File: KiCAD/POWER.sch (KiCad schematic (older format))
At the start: 9 parts, among them J35 Conn_01x02, J36 Conn_01x02, T1 da2303, U12 SN6505A

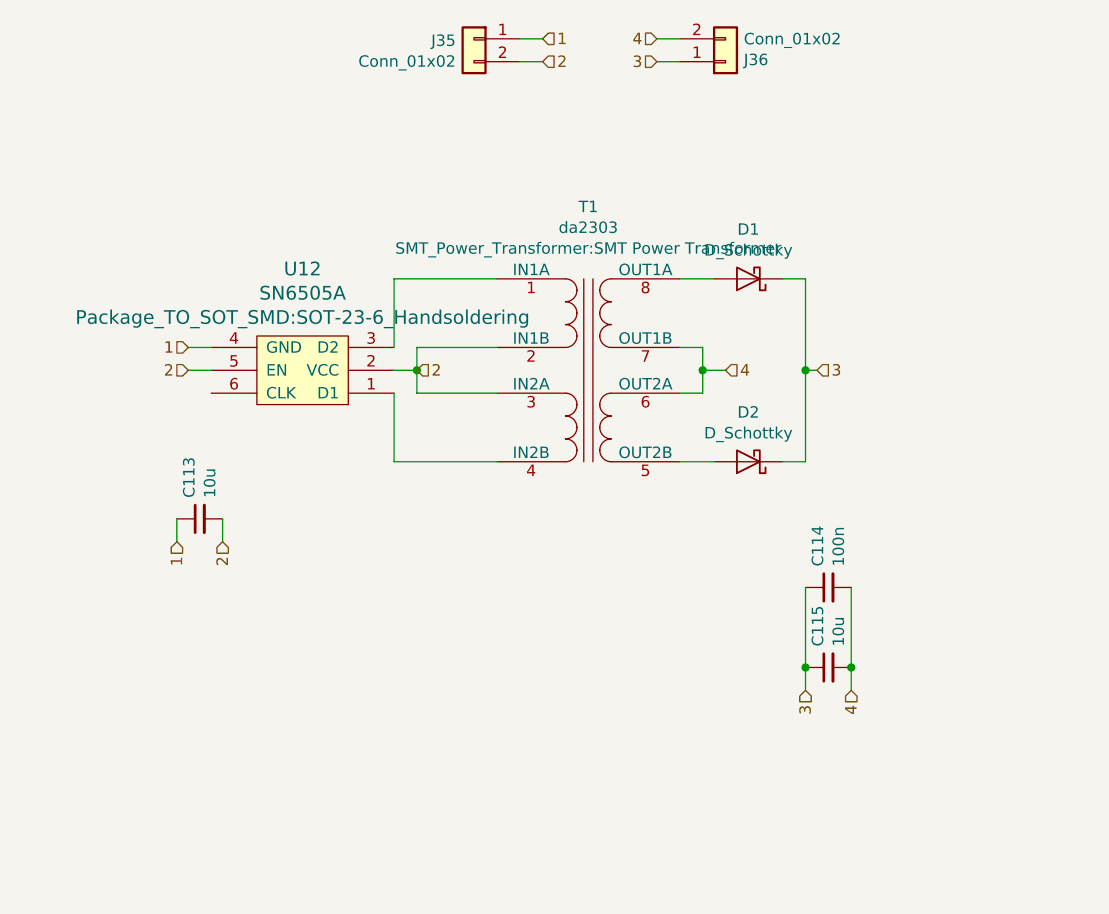
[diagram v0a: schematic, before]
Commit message: added usb, crystals
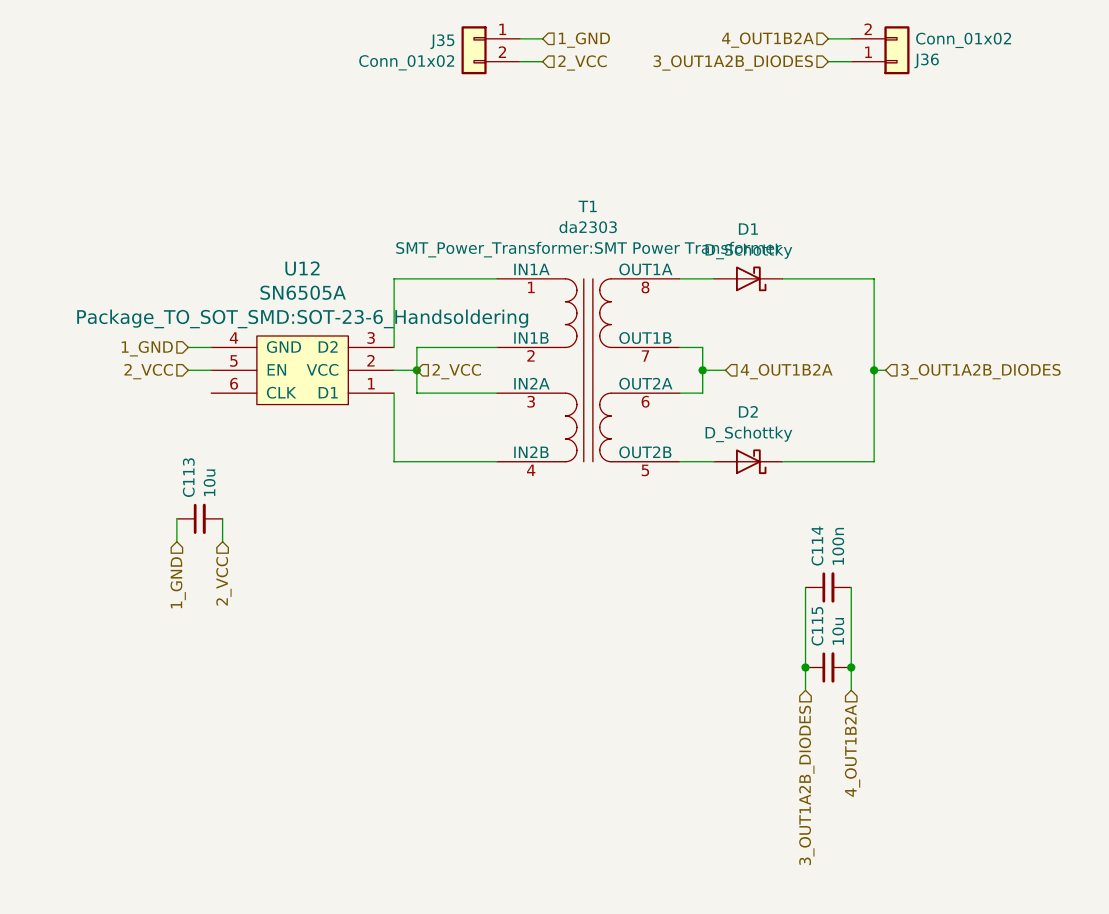
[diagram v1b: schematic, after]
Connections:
- net 1 renamed 1_GND
- net 2 renamed 2_VCC
- net 3 renamed 3_OUT1A2B_DIODES
- net 4 renamed 4_OUT1B2A
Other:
- moved on the sheet: J36
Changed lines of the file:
@@
 $Descr A4 11693 8268
 encoding utf-8
-Sheet 13 17
+Sheet 12 18
 Title ""
 Date ""
@@
 $EndComp
 Text HLabel 5350 4650 3    50   Input ~ 0
-3
+3_OUT1A2B_DIODES
 Text HLabel 5550 4650 3    50   Input ~ 0
-4
+4_OUT1B2A
 $Comp
 L Device:C_Small C?
@@
 Connection ~ 5550 4550
 Text HLabel 2600 4000 3    50   Input ~ 0
-1
+1_GND
 Text HLabel 2800 4000 3    50   Input ~ 0
-2
+2_VCC
 $Comp
 L Device:C_Small C?
@@
 L Connector_Generic:Conn_01x02 J?
 U 1 1 5CDCDD1E
-P 5000 1900
+P 5750 1900
 AR Path="/5CDAD75F/5CDCDD1E" Ref="J?"  Part="1"
 AR Path="/5CDCD748/5CDCDD1E" Ref="J36"  Part="1"
-F 0 "J36" H 5080 1892 50  0000 L CNN
-F 1 "Conn_01x02" H 5080 1801 50  0000 L CNN
-F 2 "Connector_PinHeader_2.54mm:PinHeader_1x02_P2.54mm_Vertical" H 5000 1900 50  0001 C CNN
-F 3 "~" H 5000 1900 50  0001 C CNN
-	1    5000 1900
+F 0 "J36" H 5830 1892 50  0000 L CNN
+F 1 "Conn_01x02" H 5830 1801 50  0000 L CNN
+F 2 "Connector_PinHeader_2.54mm:PinHeader_1x02_P2.54mm_Vertical" H 5750 1900 50  0001 C CNN
+F 3 "~" H 5750 1900 50  0001 C CNN
+	1    5750 1900
 	1    0    0    1
 $EndComp
@@
 $EndComp
 Text HLabel 4200 1900 2    50   Input ~ 0
-2
+2_VCC
 Text HLabel 4200 1800 2    50   Input ~ 0
-1
+1_GND
 Wire Wire Line
 	4200 1900 4100 1900
 Wire Wire Line
 	4200 1800 4100 1800
-Text HLabel 4700 1900 0    50   Input ~ 0
-3
-Wire Wire Line
-	4700 1900 4800 1900
-Text HLabel 4700 1800 0    50   Input ~ 0
-4
-Wire Wire Line
-	4700 1800 4800 1800
+Text HLabel 5450 1900 0    50   Input ~ 0
+3_OUT1A2B_DIODES
+Wire Wire Line
+	5450 1900 5550 1900
+Text HLabel 5450 1800 0    50   Input ~ 0
+4_OUT1B2A
+Wire Wire Line
+	5450 1800 5550 1800
 Text HLabel 2650 3150 0    50   Input ~ 0
-1
+1_GND
 Text HLabel 2650 3250 0    50   Input ~ 0
-2
+2_VCC
 Wire Wire Line
 	2650 3150 2750 3150
@@
 	2650 3250 2750 3250
 Text HLabel 3650 3250 2    50   Input ~ 0
-2
+2_VCC
 Wire Wire Line
 	3650 3250 3550 3250
@@
 Wire Wire Line
 	4900 3350 4800 3350
-Text HLabel 5400 3250 2    50   Input ~ 0
-3
+Text HLabel 5700 3250 2    50   Input ~ 0
+3_OUT1A2B_DIODES
 Text HLabel 5000 3250 2    50   Input ~ 0
-4
+4_OUT1B2A
 Wire Wire Line
 	4900 3250 5000 3250
@@
 	4900 3250 4900 3350
 Wire Wire Line
-	5250 2850 5350 2850
-Wire Wire Line
-	5350 3250 5400 3250
-Wire Wire Line
-	5350 3650 5250 3650
-Connection ~ 5350 3250
-Wire Wire Line
-	5350 3250 5350 3650
-Wire Wire Line
-	5350 2850 5350 3250
+	5650 3250 5700 3250
+Connection ~ 5650 3250
+Wire Wire Line
+	5650 3250 5650 3650
+Wire Wire Line
+	5650 2850 5650 3250
+Wire Wire Line
+	5250 2850 5650 2850
+Wire Wire Line
+	5250 3650 5650 3650
 $EndSCHEMATC
